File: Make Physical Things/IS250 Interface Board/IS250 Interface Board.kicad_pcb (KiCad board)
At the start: 2 copper layers, 175.3 x 106.7 mm, 52 parts, among them J1 24_Pin_Reorg, J2 16_Pin, J3 Barrel_Jack, J4 XT60-M, J5 Conn_01x02, J6 Conn_01x02, J7 Conn_01x02, J8 Conn_01x02, Q1 PN2222A, Q10 PN2222A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

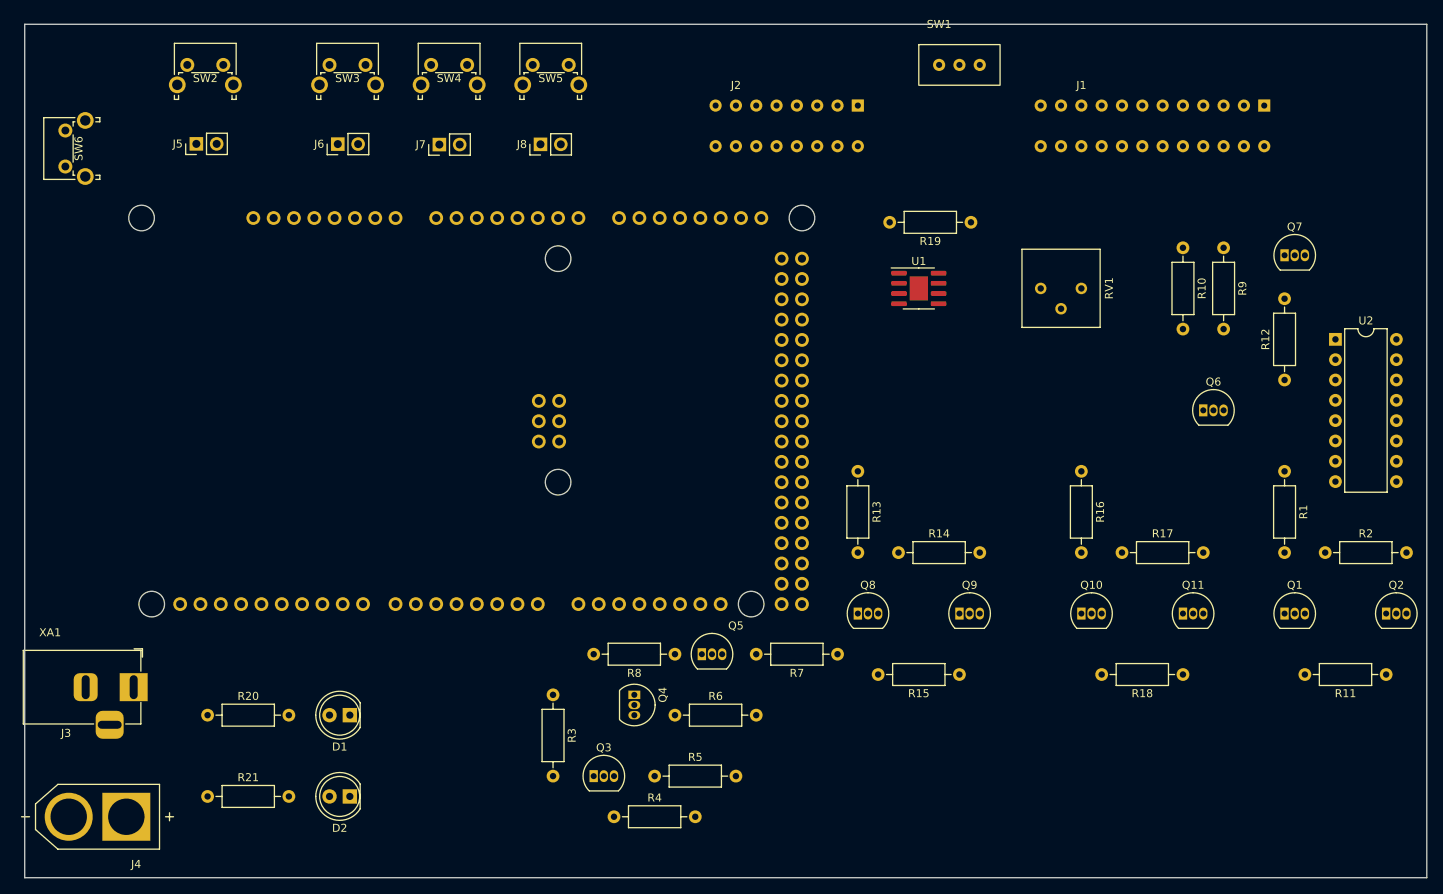
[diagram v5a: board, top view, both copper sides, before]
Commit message: PCB routing and Test Points
The routing for the PCB is complete, and I have added test points for the waveforms
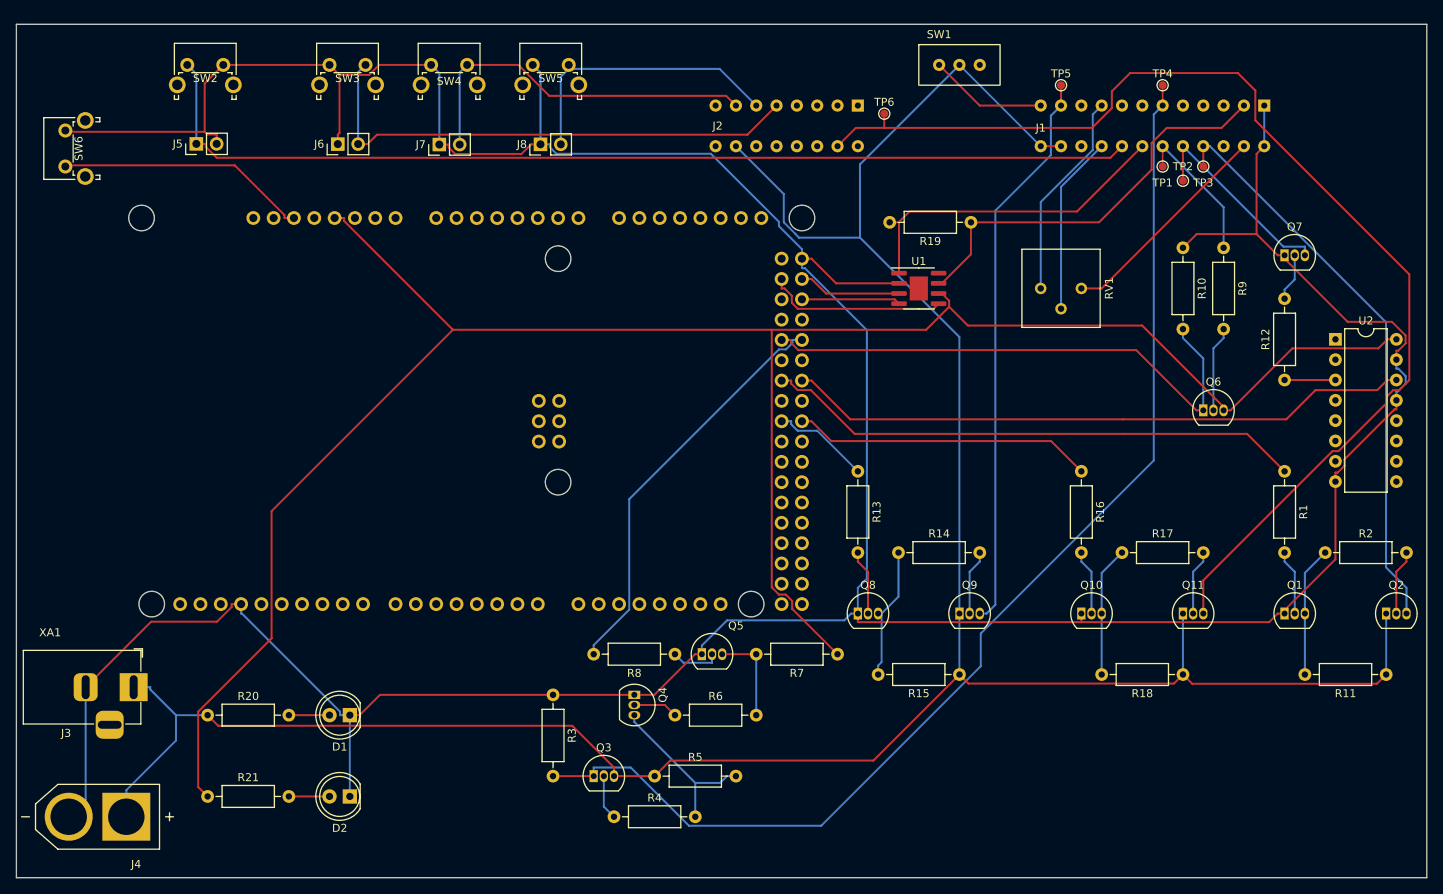
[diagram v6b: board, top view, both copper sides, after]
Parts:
- added TP1: TestPoint_Pad_D1.0mm, TestPoint:TestPoint_Pad_D1.0mm, F.Cu at (208.3, 58.4)
- added TP2: TestPoint_Pad_D1.0mm, TestPoint:TestPoint_Pad_D1.0mm, F.Cu at (210.8, 60.2)
- added TP3: TestPoint_Pad_D1.0mm, TestPoint:TestPoint_Pad_D1.0mm, F.Cu at (213.4, 58.4)
- added TP4: TestPoint_Pad_D1.0mm, TestPoint:TestPoint_Pad_D1.0mm, F.Cu at (208.3, 48.3)
- added TP5: TestPoint_Pad_D1.0mm, TestPoint:TestPoint_Pad_D1.0mm, F.Cu at (195.6, 48.3)
- added TP6: TestPoint_Pad_D1.0mm, TestPoint:TestPoint_Pad_D1.0mm, F.Cu at (173.5, 51.8)
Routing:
- net GND: track 0.00 -> 491.9 mm
- net +12V: track 0.00 -> 325.4 mm
- net +5V: track 0.00 -> 268.3 mm
- net /MPX Transciever/MPX+: track 0.00 -> 147.9 mm
- net /RHT-TRN: track 0.00 -> 144.8 mm
- net Net-(J1-Pad20): track 0.00 -> 127.6 mm
- net /Speedo: track 0.00 -> 78.3 mm
- net /Tacho Conversion/12V Out: track 0.00 -> 72.0 mm
- net /LFT-TRN: track 0.00 -> 70.7 mm
- net /MPX-R: track 0.00 -> 67.8 mm
- net /Tacho: track 0.00 -> 67.8 mm
- net /Satellite Switch/RSEL: track 0.00 -> 64.6 mm
- net /Fuel System/FUEL-GND: track 0.00 -> 51.7 mm
- net /MPX-S: track 0.00 -> 51.3 mm
- net /Satellite Switch/SET: track 0.00 -> 46.0 mm
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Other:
- board size 175.3 x 106.7 mm -> 176.3 x 106.7 mm

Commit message: Finalised Layout and Silkscreen
Finished all of the PCB design, added the test points and silkscreen.
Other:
- board text added: "+12v"
- board text added: "12V POWER"
- board text added: "5V POWER"
- board text added: "Backlight Dimmer"
- board text added: "CREATED BY MRARGON39 DON'T COPY THIS SHIT"
- board text added: "DISP"
- board text added: "DISP-SW"
- board text added: "FUEL"
- board text added: "FUEL-GND"
- board text added: "GND"
- board text added: "IGN"
- board text added: "ILL+"
- board text added: "ILL-GND"
- board text added: "ILL-SENSE"
- board text added: "LEFT"
- board text added: "LEFT-TURN"
- board text added: "LFT-TRN"
- board text added: "MPX+"
- board text added: "MPX-"
- board text added: "MPX-R"
- board text added: "MPX-SEND"
- board text added: "RESET"
- board text added: "RHT-TRN"
- board text added: "RIGHT"
- board text added: "RIGHT-TURN"
- board text added: "SET"
- board text added: "SPD-IN"
- board text added: "Speed"
- board text added: "TACH"
- board text added: "TACHO"

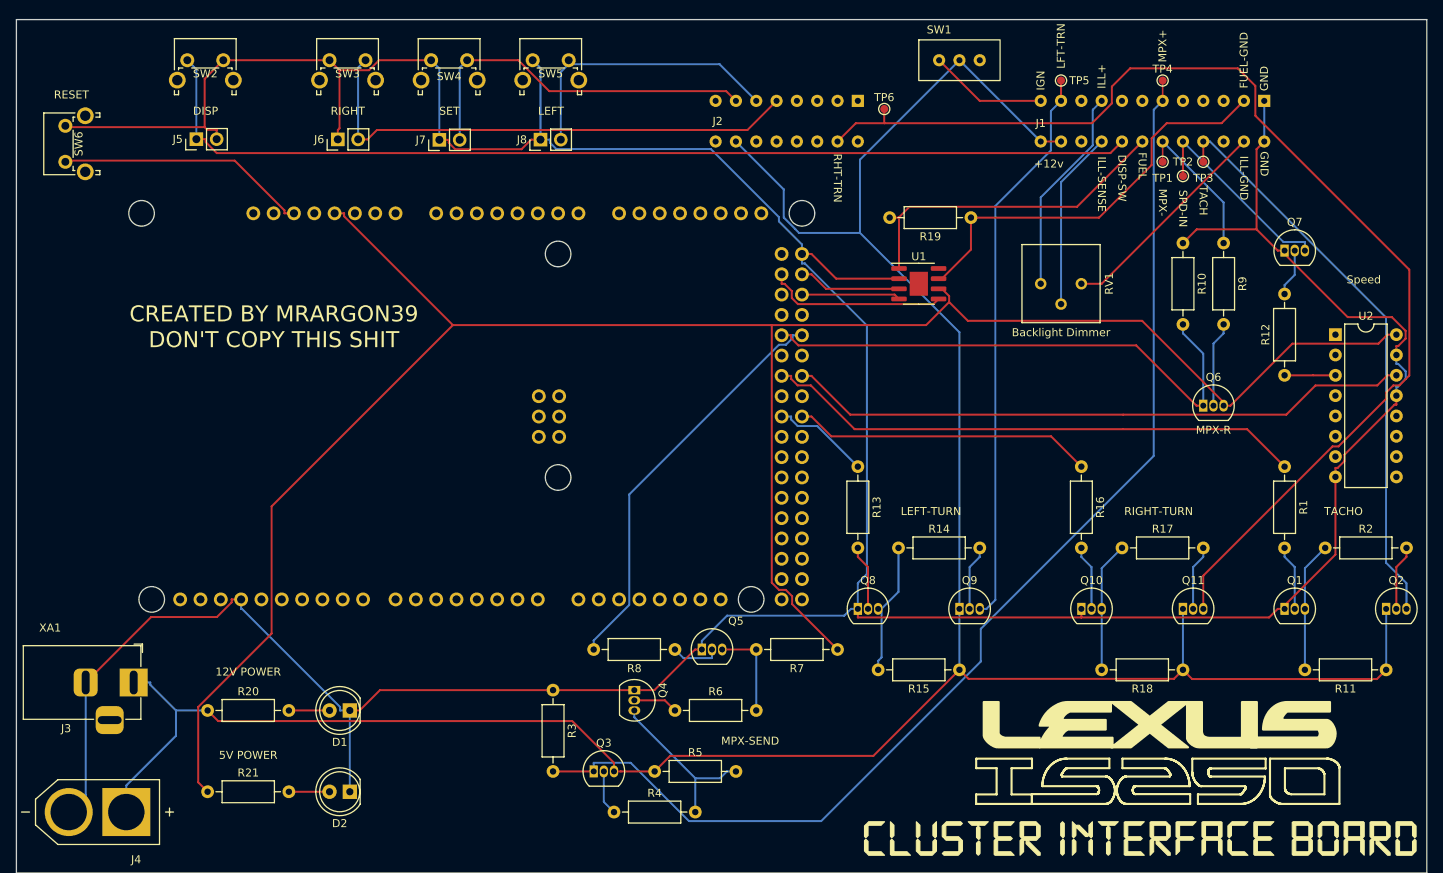
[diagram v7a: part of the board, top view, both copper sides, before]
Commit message: Added mounting holes
Added M3 Holes for standoffs, for mounting in an enclosure or to keep it off a desk
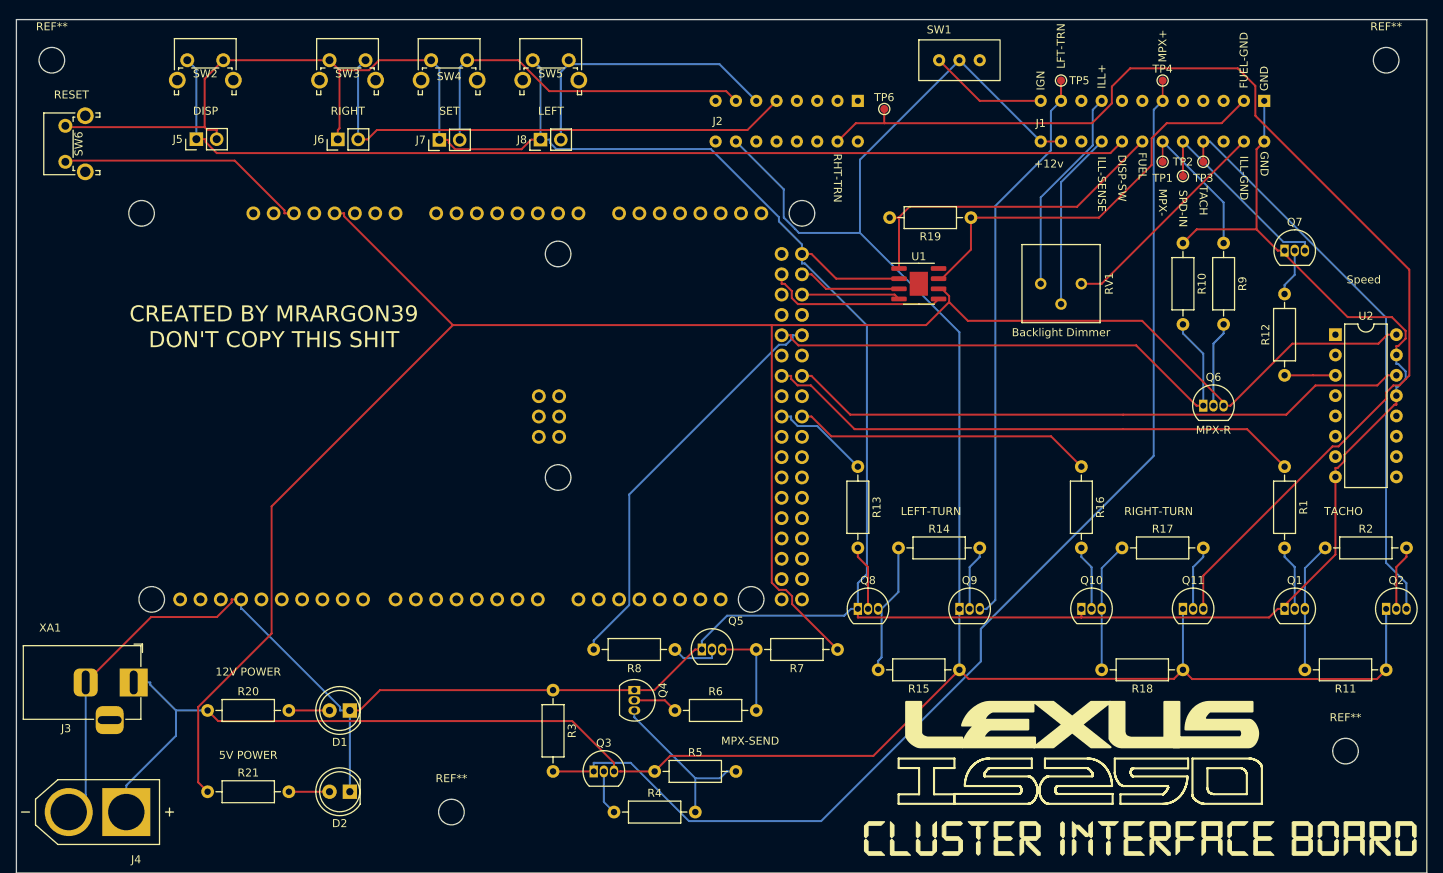
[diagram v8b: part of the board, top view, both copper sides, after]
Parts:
- added REF**: MountingHole_3.2mm_M3, MountingHole:MountingHole_3.2mm_M3, F.Cu at (69.4, 45.7)
- added REF**: MountingHole_3.2mm_M3, MountingHole:MountingHole_3.2mm_M3, F.Cu at (119.4, 139.7)
- added REF**: MountingHole_3.2mm_M3, MountingHole:MountingHole_3.2mm_M3, F.Cu at (236.2, 45.7)
- added REF**: MountingHole_3.2mm_M3, MountingHole:MountingHole_3.2mm_M3, F.Cu at (231.1, 132.1)
